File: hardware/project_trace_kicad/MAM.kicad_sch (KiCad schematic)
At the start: 5 parts, among them U501 NUCLEO-H753ZI

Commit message: Changes to Digital
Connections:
- net SPI1.NSS: no longer U501.7_17 (PA4)
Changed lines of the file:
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@@
-	(wire
-		(pts
-			(xy 132.08 60.96) (xy 133.35 60.96)
-		)
-		(stroke
-			(width 0)
-			(type default)
-		)
-	)
 	(wire
 		(pts
@@
 	(hierarchical_label "SPI1.NSS"
 		(shape output)
-		(at 132.08 60.96 180)
+		(at 128.27 60.96 180)
 		(effects
 			(font

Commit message: Hardware NSS renamed to SYNC
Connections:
- net SPI1.SYNC: now reaches U501.7_17 (PA4)
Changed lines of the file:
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@@
+	(wire
+		(pts
+			(xy 132.08 60.96) (xy 133.35 60.96)
+		)
+		(stroke
+			(width 0)
+			(type default)
+		)
+	)
 	(wire
 		(pts
@@
 		)
 	)
-	(hierarchical_label "SPI1.NSS"
+	(hierarchical_label "SPI1.SYNC"
 		(shape output)
-		(at 128.27 60.96 180)
+		(at 132.08 60.96 180)
 		(effects
 			(font

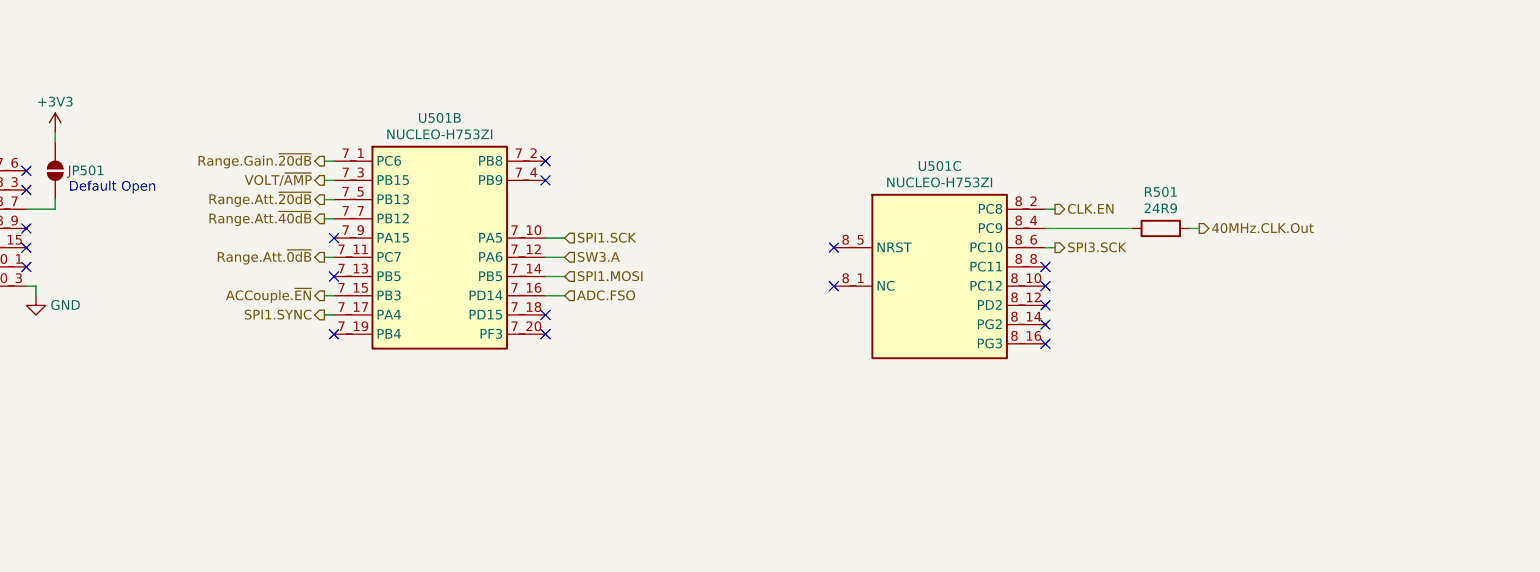
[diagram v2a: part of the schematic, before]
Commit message: Fix wrong partno, add debug LED
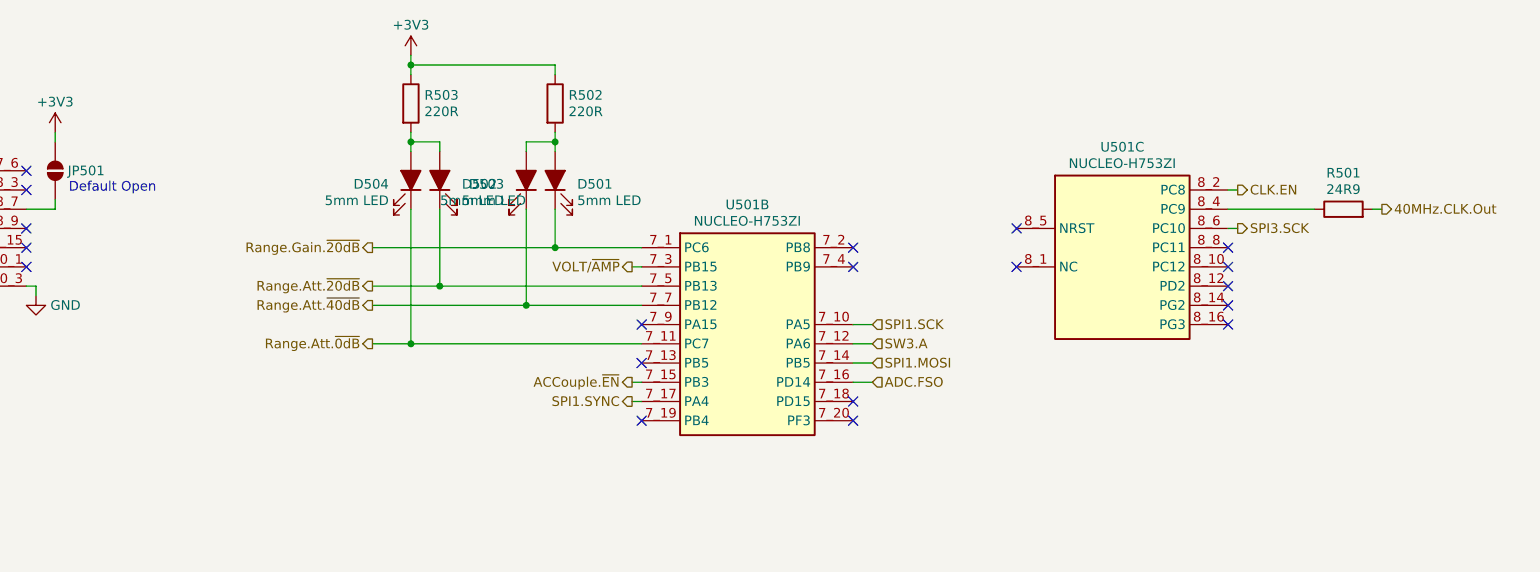
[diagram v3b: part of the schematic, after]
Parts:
- added D501, D502, D503, D504: 5mm LED, LED_THT:LED_D5.0mm, symbol Device:LED_Filled
- added R502, R503: 220R, symbol Device:R
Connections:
- net +3V3: now also R502.1, R503.1
- net Range.Att.~{0dB}: now also D504.1 (K)
- net Range.Att.~{20dB}: now also D502.1 (K)
- net Range.Att.~{40dB}: now also D503.1 (K)
- net Range.Gain.~{20dB}: now also D501.1 (K)
- new net: D501.2 (A), D503.2 (A), R502.2
- new net: D502.2 (A), D504.2 (A), R503.2
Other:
- moved on the sheet: R501, U501B, U501C

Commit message: Unfinished change of UI connectivity
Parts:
- renumbered D504 to D501, D501 to D504, R503 to R501, R501 to R503
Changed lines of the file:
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@@
 		(dnp no)
 		(fields_autoplaced yes)
-		(property "Reference" "R501"
+		(property "Reference" "R503"
 			(at 266.7 42.2146 90)
 			(show_name no)
@@
 			(project "project_trace_kicad"
 				(path "/af51f4e5-b952-4b0e-baf2-78a72fb86fcd/aebaf62e-54ce-46f5-a91f-d86d07c0b2fa"
-					(reference "R501")
+					(reference "R503")
 					(unit 1)
 				)
@@
 		(dnp no)
 		(fields_autoplaced yes)
-		(property "Reference" "R503"
+		(property "Reference" "R501"
 			(at 145.288 31.9362 0)
 			(show_name no)
@@
 			(project "project_trace_kicad"
 				(path "/af51f4e5-b952-4b0e-baf2-78a72fb86fcd/aebaf62e-54ce-46f5-a91f-d86d07c0b2fa"
-					(reference "R503")
+					(reference "R501")
 					(unit 1)
 				)
@@
 		(in_pos_files yes)
 		(dnp no)
-		(property "Reference" "D501"
+		(property "Reference" "D504"
 			(at 165.481 43.6837 90)
 			(show_name no)
@@
 			(project "project_trace_kicad"
 				(path "/af51f4e5-b952-4b0e-baf2-78a72fb86fcd/aebaf62e-54ce-46f5-a91f-d86d07c0b2fa"
-					(reference "D501")
+					(reference "D504")
 					(unit 1)
 				)
@@
 		(in_pos_files yes)
 		(dnp no)
-		(property "Reference" "D504"
+		(property "Reference" "D501"
 			(at 140.589 43.6837 90)
 			(show_name no)
@@
 			(project "project_trace_kicad"
 				(path "/af51f4e5-b952-4b0e-baf2-78a72fb86fcd/aebaf62e-54ce-46f5-a91f-d86d07c0b2fa"
-					(reference "D504")
+					(reference "D501")
 					(unit 1)
 				)

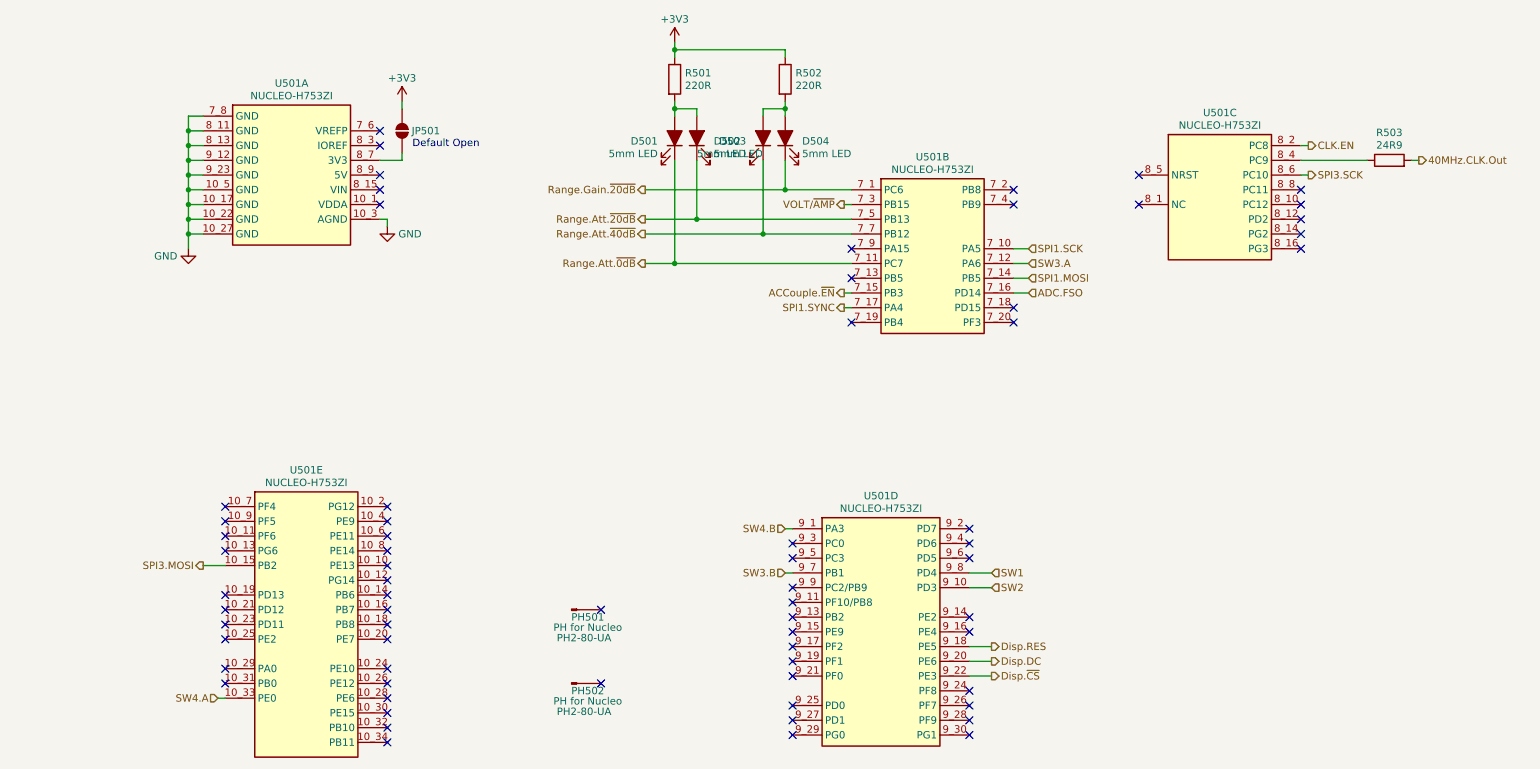
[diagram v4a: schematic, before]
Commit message: Review 1 issues adressed
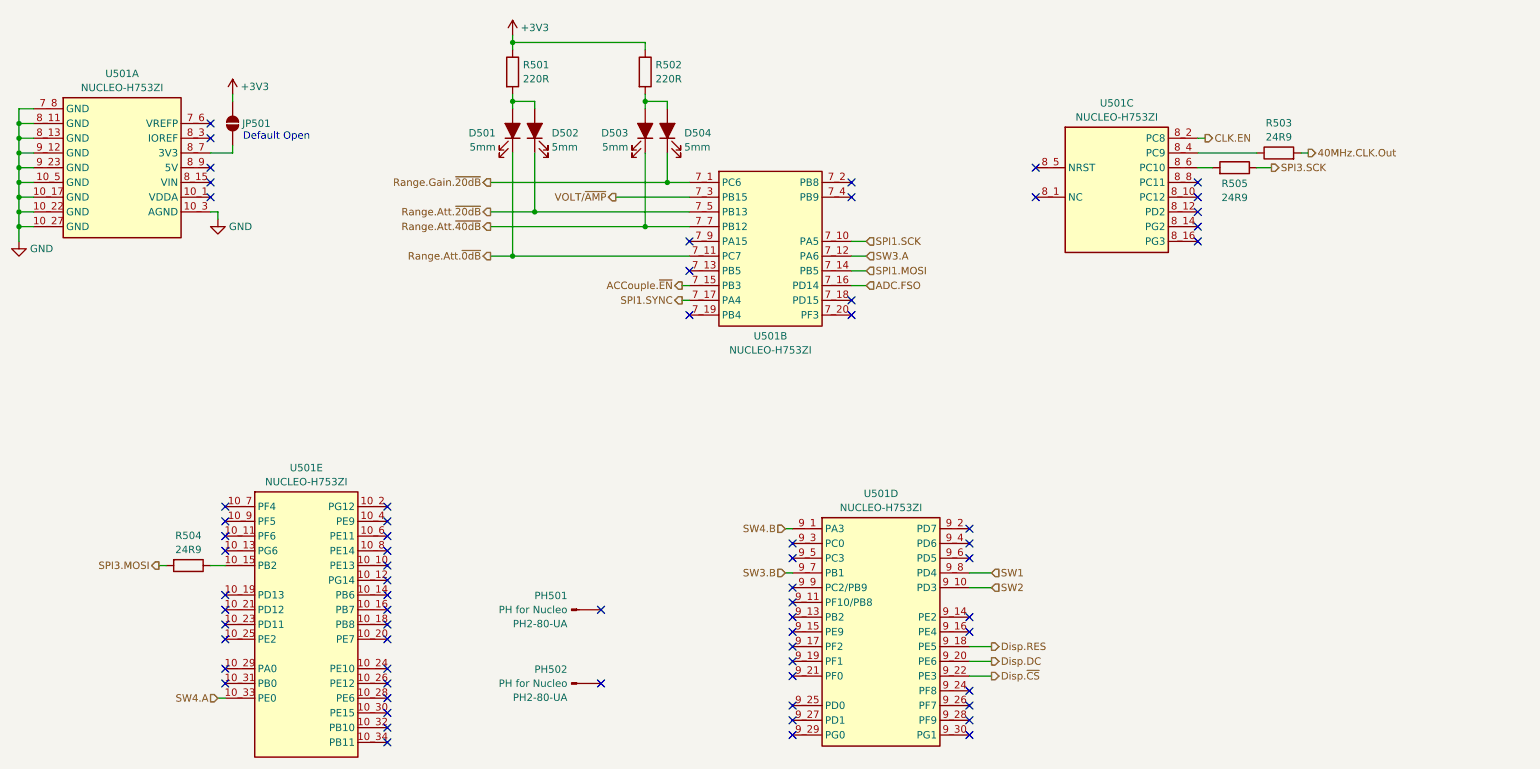
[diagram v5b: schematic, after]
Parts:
- added R504, R505: 24R9, Resistor_SMD:R_0603_1608Metric_Pad0.98x0.95mm_HandSolder, symbol Device:R
- D501, D502, D503, D504: value 5mm LED -> 5mm
- R501: footprint (none) -> Resistor_THT:R_Axial_DIN0207_L6.3mm_D2.5mm_P10.16mm_Horizontal; DigikeyPN (none) -> N/A
- R502: DigikeyPN (none) -> N/A
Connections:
- net SPI3.MOSI: now also R504.2; no longer U501.10_15 (PB2)
- net SPI3.SCK: now also R505.1; no longer U501.8_6 (PC10)
- new net: R505.2, U501.8_6 (PC10)
- new net: R504.1, U501.10_15 (PB2)
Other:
- moved on the sheet: D501, D502, D503, D504, JP501, R501, R502, R503, U501A, U501B, U501C
